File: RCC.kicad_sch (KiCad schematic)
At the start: 42 parts, among them J1 Battery, J2 USB_C_Receptacle_USB2.0_16P, J3 Conn_01x07, J4 Conn_01x04_Pin, SW2 SW_Push, U1 BQ24040DGQR, U2 ESD7104MUTAG, U3 TLV75801PDRV, U5 STM32L412KBTx

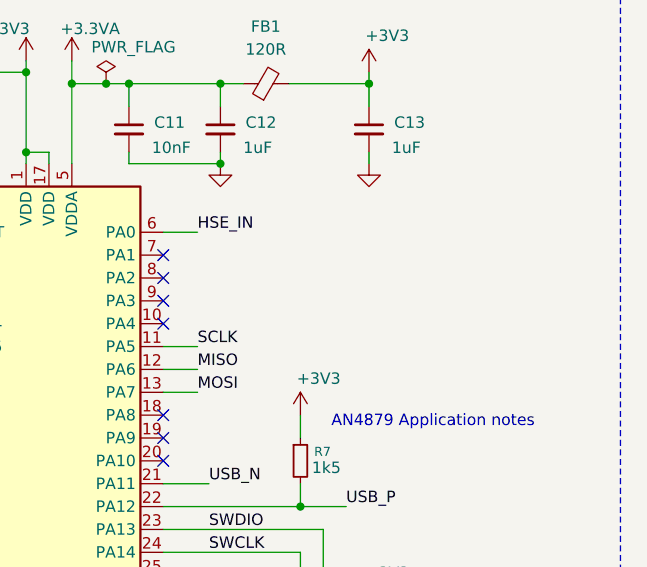
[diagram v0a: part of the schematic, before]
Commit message: Add crystal in schematic and pcb
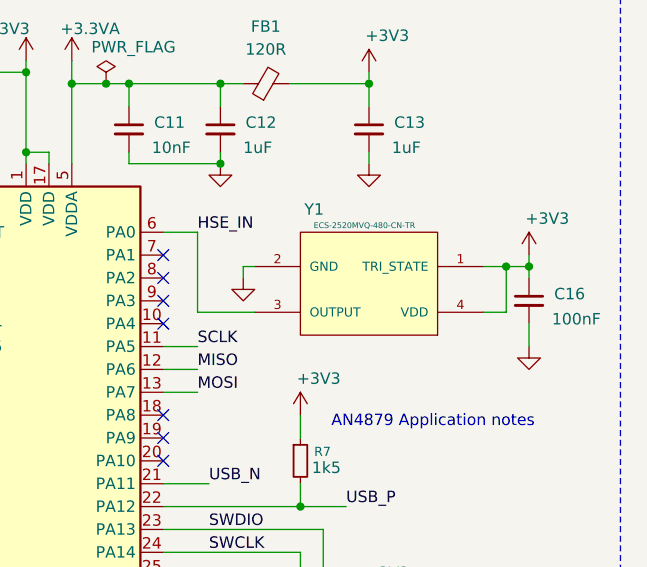
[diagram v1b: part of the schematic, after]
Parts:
- added C16: 100nF, Capacitor_SMD:C_0603_1608Metric, symbol Device:C_Small
- added Y1: ECS-2520MVQ-480-CN-TR, ECS_2520MVQ_480_CN_TR:OSC_ECS-2520S25-250-FN-TR, symbol ECS-2520MVQ-480-CN-TR:ECS-2520MVQ-480-CN-TR
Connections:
- net +3V3: now also C16.1, Y1.1 (TRI_STATE), Y1.4 (VDD)
- net GND: now also C16.2, Y1.2 (GND)
- net HSE_IN: now also Y1.3 (OUTPUT)

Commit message: Finalise PCB and add 3d models
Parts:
- added D4: LED_Small, LED_SMD:LED_0603_1608Metric, symbol Device:LED_Small
- J4: footprint Connector_JST:JST_EH_B4B-EH-A_1x04_P2.50mm_Vertical -> Connector_JST:JST_EH_S4B-EH_1x04_P2.50mm_Horizontal
- R11: value 0 -> 1k
- R7: now not fitted
- U2: footprint ESD7104:UDFN10_ONS -> UDFN10_ONS
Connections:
- net CHG_STATUS: now also U5.27 (PB4)
- net DIS_CS: now also U5.30 (PB7)
- net DIS_DC: now also U5.29 (PB6)
- net DIS_RST: now also U5.28 (PB5)
- net GND: now also D4.1 (K); no longer R11.2
- net GYRO_CS: now also U5.14 (PB0)
- net GY_INT1: now also U5.10 (PA4)
- net GY_INT2: now also U5.15 (PB1)
- net SWCLK: now also J4.2 (Pin_2); no longer J4.3 (Pin_3)
- net SWDIO: now also J4.3 (Pin_3); no longer J4.2 (Pin_2)
- net VBUS: now also U2.5 (I/O), U2.6 (NC); no longer U2.4 (I/O), U2.7 (NC)
- net at J2.S1 (SHIELD): no longer R11.1
- net TEST_LED: now reaches U5.18 (PA8)
- net TEST_LED: now also R11.2
- new net: D4.2 (A), R11.1
- no-connect marks 25 -> 19
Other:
- note removed: "Connect CC line? 5k11"
- note removed: "TODO: - SPI CSs - GPIOs (display and inter - HSE clock (0-48MHz) - Status LEDs"
- note removed: "TODO: Calculate resistance and cutoff load when charging"
- moved on the sheet: C1, C10, C11, C12, C13, C14, C15, C16, C2, C8, C9, D2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

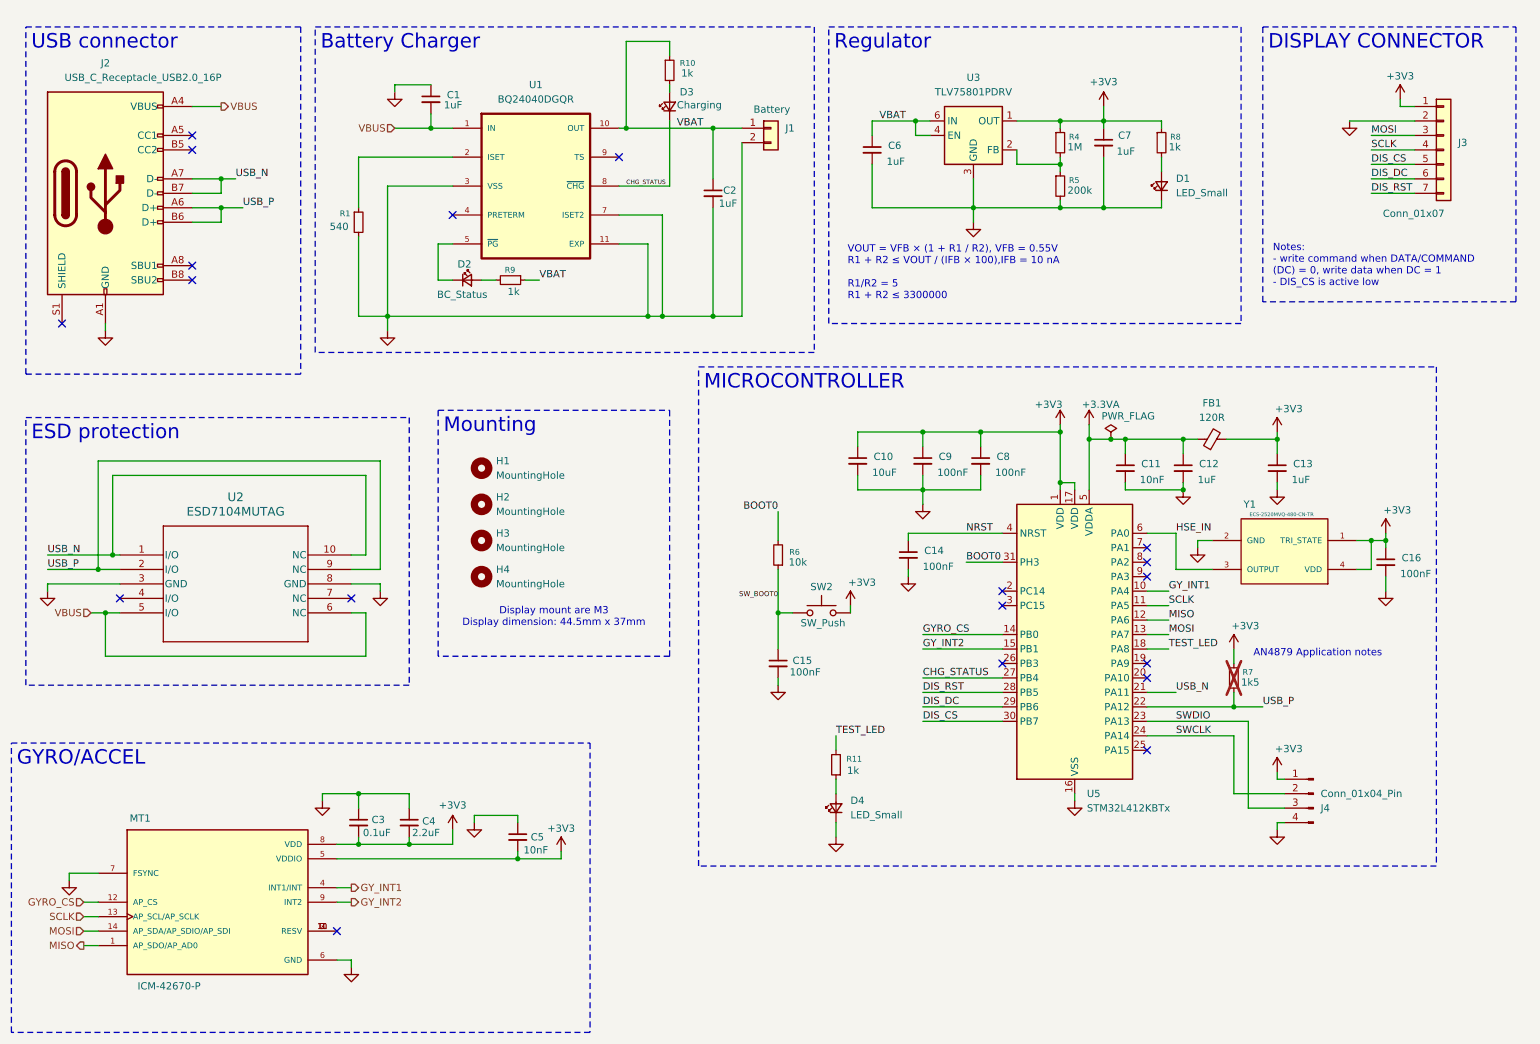
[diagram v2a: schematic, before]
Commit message: Change connectors to jst-ph
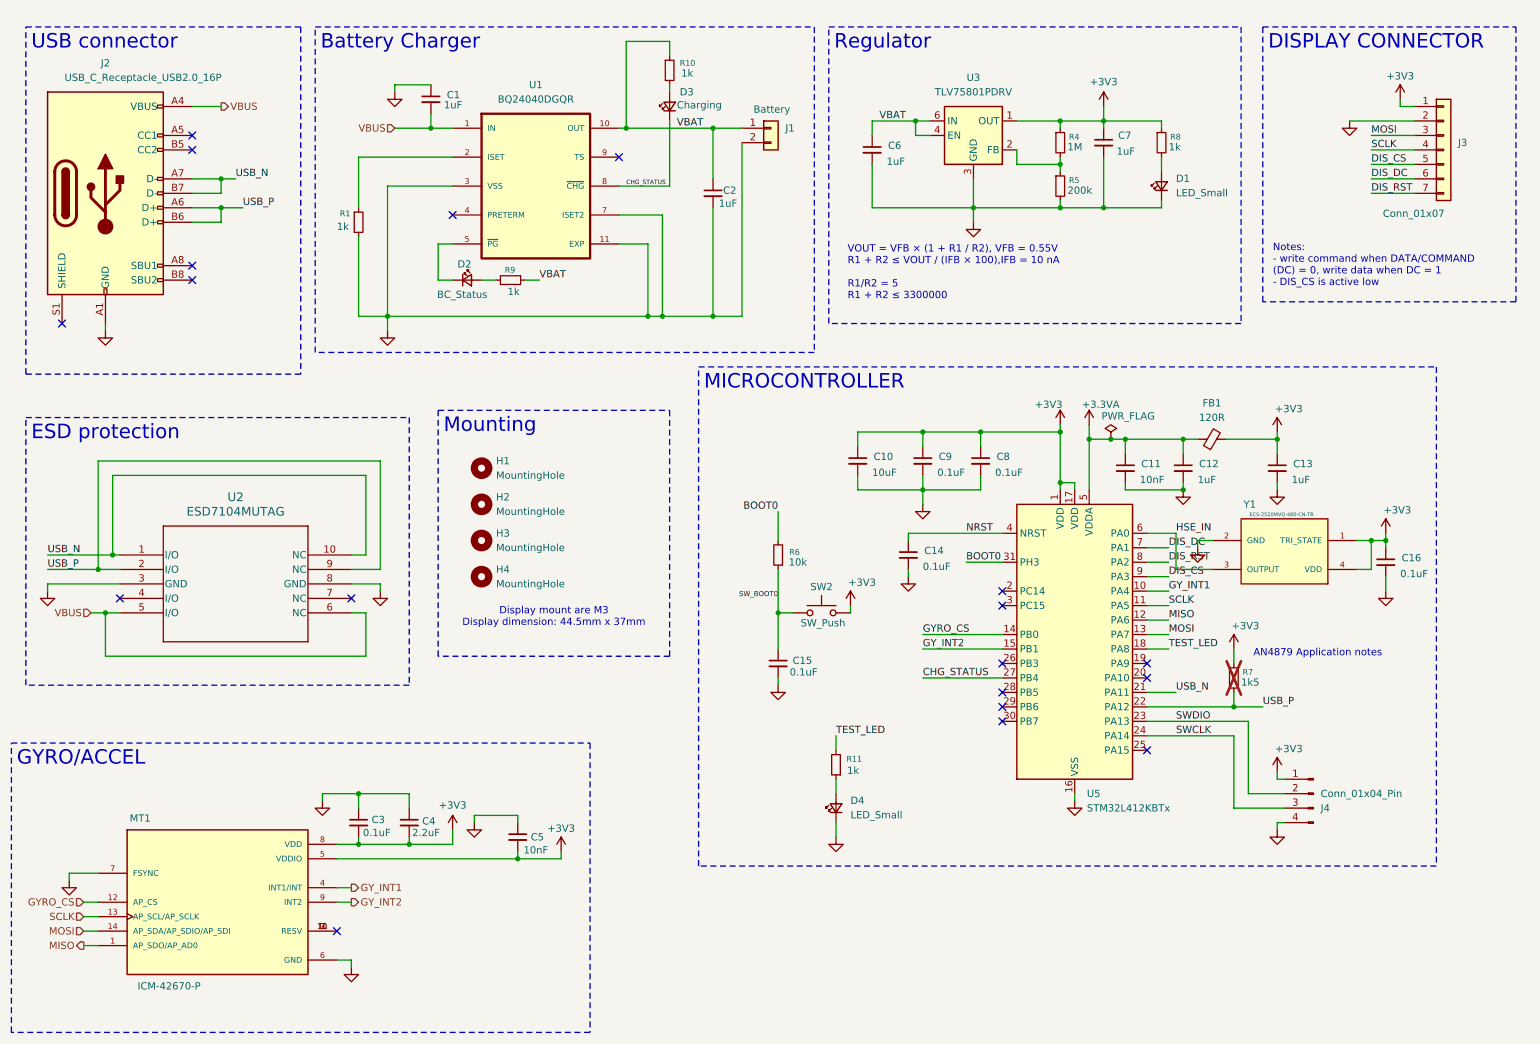
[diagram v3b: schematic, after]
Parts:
- C14, C15, C16, C8, C9: value 100nF -> 0.1uF
- J1: footprint Connector_JST:JST_EH_S2B-EH_1x02_P2.50mm_Horizontal -> Connector_JST:JST_PH_S2B-PH-K_1x02_P2.00mm_Horizontal
- J3: footprint Connector_JST:JST_EH_S7B-EH_1x07_P2.50mm_Horizontal -> Connector_JST:JST_PH_S7B-PH-K_1x07_P2.00mm_Horizontal
- J4: footprint Connector_JST:JST_EH_S4B-EH_1x04_P2.50mm_Horizontal -> Connector_JST:JST_PH_S4B-PH-K_1x04_P2.00mm_Horizontal
- R1: value 540 -> 1k
- U2: footprint UDFN10_ONS -> ESD7104:UDFN10_ONS
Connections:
- net DIS_CS: now also U5.9 (PA3); no longer U5.30 (PB7)
- net DIS_DC: now also U5.7 (PA1); no longer U5.29 (PB6)
- net DIS_RST: now also U5.8 (PA2); no longer U5.28 (PB5)
- net SWCLK: now also J4.3 (Pin_3); no longer J4.2 (Pin_2)
- net SWDIO: now also J4.2 (Pin_2); no longer J4.3 (Pin_3)
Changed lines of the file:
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@@
 	)
 	(no_connect
+		(at 189.23 135.89)
+	)
+	(no_connect
 		(at 214.63 143.51)
 	)
 	(no_connect
+		(at 189.23 133.35)
+	)
+	(no_connect
 		(at 46.99 60.96)
 	)
@@
 	)
 	(no_connect
-		(at 214.63 107.95)
-	)
-	(no_connect
 		(at 92.71 49.53)
 	)
@@
 	)
 	(no_connect
-		(at 214.63 113.03)
-	)
-	(no_connect
 		(at 46.99 38.1)
 	)
@@
 	)
 	(no_connect
-		(at 214.63 110.49)
+		(at 189.23 128.27)
 	)
 	(no_connect
-		(at 189.23 128.27)
+		(at 189.23 138.43)
 	)
 	(no_connect
@@
 	(wire
 		(pts
+			(xy 229.87 153.67) (xy 238.76 153.67)
+		)
+		(stroke
+			(width 0)
+			(type default)
+		)
+	)
+	(wire
+		(pts
 			(xy 185.42 87.63) (xy 185.42 90.17)
 		)
@@
 	(wire
 		(pts
-			(xy 175.26 135.89) (xy 189.23 135.89)
-		)
-		(stroke
-			(width 0)
-			(type default)
-		)
-	)
-	(wire
-		(pts
 			(xy 175.26 123.19) (xy 189.23 123.19)
 		)
@@
 	(wire
 		(pts
+			(xy 214.63 113.03) (xy 218.44 113.03)
+		)
+		(stroke
+			(width 0)
+			(type default)
+		)
+	)
+	(wire
+		(pts
 			(xy 163.83 97.79) (xy 175.26 97.79)
 		)
@@
 	(wire
 		(pts
+			(xy 232.41 138.43) (xy 232.41 151.13)
+		)
+		(stroke
+			(width 0)
+			(type default)
+		)
+	)
+	(wire
+		(pts
 			(xy 149.86 101.6) (xy 149.86 106.68)
 		)
@@
 	(wire
 		(pts
+			(xy 214.63 110.49) (xy 218.44 110.49)
+		)
+		(stroke
+			(width 0)
+			(type default)
+		)
+	)
+	(wire
+		(pts
 			(xy 172.72 111.76) (xy 172.72 113.03)
 		)
@@
 	(wire
 		(pts
-			(xy 90.17 54.61) (xy 90.17 60.96)
+			(xy 232.41 151.13) (xy 238.76 151.13)
 		)
 		(stroke
@@
 	(wire
 		(pts
-			(xy 214.63 120.65) (xy 218.44 120.65)
+			(xy 90.17 54.61) (xy 90.17 60.96)
 		)
 		(stroke
@@
 	(wire
 		(pts
-			(xy 21.59 111.76) (xy 30.48 111.76)
+			(xy 214.63 120.65) (xy 218.44 120.65)
 		)
 		(stroke
@@
 	(wire
 		(pts
-			(xy 92.71 39.37) (xy 76.2 39.37)
+			(xy 21.59 111.76) (xy 30.48 111.76)
 		)
 		(stroke
@@
 	(wire
 		(pts
-			(xy 127 54.61) (xy 121.92 54.61)
+			(xy 92.71 39.37) (xy 76.2 39.37)
 		)
 		(stroke
@@
 	(wire
 		(pts
-			(xy 104.14 161.29) (xy 104.14 162.56)
+			(xy 127 54.61) (xy 121.92 54.61)
 		)
 		(stroke
@@
 	(wire
 		(pts
-			(xy 232.41 153.67) (xy 238.76 153.67)
+			(xy 104.14 161.29) (xy 104.14 162.56)
 		)
 		(stroke
@@
 	(wire
 		(pts
-			(xy 123.19 34.29) (xy 138.43 34.29)
+			(xy 214.63 107.95) (xy 218.44 107.95)
 		)
 		(stroke
@@
 	(wire
 		(pts
-			(xy 229.87 140.97) (xy 229.87 151.13)
+			(xy 123.19 34.29) (xy 138.43 34.29)
 		)
 		(stroke
@@
 	(wire
 		(pts
-			(xy 214.63 123.19) (xy 218.44 123.19)
+			(xy 229.87 140.97) (xy 229.87 153.67)
 		)
 		(stroke
@@
 	(wire
 		(pts
-			(xy 34.29 114.3) (xy 21.59 114.3)
+			(xy 214.63 123.19) (xy 218.44 123.19)
 		)
 		(stroke
@@
 	(wire
 		(pts
-			(xy 175.26 133.35) (xy 189.23 133.35)
+			(xy 34.29 114.3) (xy 21.59 114.3)
 		)
 		(stroke
@@
 	(wire
 		(pts
-			(xy 175.26 138.43) (xy 189.23 138.43)
-		)
-		(stroke
-			(width 0)
-			(type default)
-		)
-	)
-	(wire
-		(pts
-			(xy 229.87 151.13) (xy 238.76 151.13)
-		)
-		(stroke
-			(width 0)
-			(type default)
-		)
-	)
-	(wire
-		(pts
 			(xy 237.49 147.32) (xy 237.49 148.59)
 		)
@@
 	(wire
 		(pts
-			(xy 229.87 135.89) (xy 234.95 135.89)
-		)
-		(stroke
-			(width 0)
-			(type default)
-		)
-	)
-	(wire
-		(pts
 			(xy 207.01 33.02) (xy 217.17 33.02)
 		)
@@
 	(wire
 		(pts
-			(xy 232.41 138.43) (xy 232.41 153.67)
-		)
-		(stroke
-			(width 0)
-			(type default)
-		)
-	)
-	(wire
-		(pts
 			(xy 229.87 133.35) (xy 229.87 135.89)
 		)
@@
 	(wire
 		(pts
-			(xy 214.63 138.43) (xy 232.41 138.43)
+			(xy 229.87 135.89) (xy 234.95 135.89)
 		)
 		(stroke
@@
 	(wire
 		(pts
+			(xy 214.63 138.43) (xy 232.41 138.43)
+		)
+		(stroke
+			(width 0)
+			(type default)
+		)
+	)
+	(wire
+		(pts
 			(xy 226.06 106.68) (xy 223.52 106.68)
 		)
@@
 		)
 	)
-	(label "DIS_DC"
-		(at 175.26 135.89 0)
+	(label "DIS_RST"
+		(at 218.44 110.49 0)
 		(effects
 			(font
@@
 		)
 	)
-	(label "DIS_RST"
-		(at 175.26 133.35 0)
+	(label "DIS_CS"
+		(at 218.44 113.03 0)
 		(effects
 			(font
@@
 		)
 	)
-	(label "DIS_CS"
-		(at 175.26 138.43 0)
+	(label "DIS_DC"
+		(at 218.44 107.95 0)
 		(effects
 			(font
@@
 			)
 		)
-		(property "Footprint" "Connector_JST:JST_EH_S2B-EH_1x02_P2.50mm_Horizontal"
+		(property "Footprint" "Connector_JST:JST_PH_S2B-PH-K_1x02_P2.00mm_Horizontal"
 			(at 148.59 34.29 0)
 			(effects
@@
 			)
 		)
-		(property "Value" "100nF"
+		(property "Value" "0.1uF"
 			(at 259.08 112.522 0)
 			(effects
@@
 			)
 		)
-		(property "Value" "100nF"
+		(property "Value" "0.1uF"
 			(at 151.892 129.794 0)
 			(effects
@@
 			)
 		)
-		(property "Value" "100nF"
+		(property "Value" "0.1uF"
 			(at 187.96 94.742 0)
 			(effects
@@
 			)
 		)
-		(property "Footprint" "Connector_JST:JST_EH_S4B-EH_1x04_P2.50mm_Horizontal"
+		(property "Footprint" "Connector_JST:JST_PH_S4B-PH-K_1x04_P2.00mm_Horizontal"
 			(at 243.84 151.13 0)
 			(effects
@@
 			)
 		)
-		(property "Value" "540"
-			(at 71.12 51.562 0)
+		(property "Value" "1k"
+			(at 72.39 51.562 0)
 			(effects
 				(font
@@
 			)
 		)
-		(property "Value" "100nF"
+		(property "Value" "0.1uF"
 			(at 177.8 94.742 0)
 			(effects
@@
 			)
 		)
-		(property "Footprint" "Connector_JST:JST_EH_S7B-EH_1x07_P2.50mm_Horizontal"
+		(property "Footprint" "Connector_JST:JST_PH_S7B-PH-K_1x07_P2.00mm_Horizontal"
 			(at 266.7 38.1 0)
 			(effects
@@
 			)
 		)
-		(property "Value" "100nF"
+		(property "Value" "0.1uF"
 			(at 175.26 111.252 0)
 			(effects
@@
 			)
 		)
-		(property "Footprint" "UDFN10_ONS"
+		(property "Footprint" "ESD7104:UDFN10_ONS"
 			(at 34.29 109.22 0)
 			(effects

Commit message: Add termination resistor to spi and change esd protection
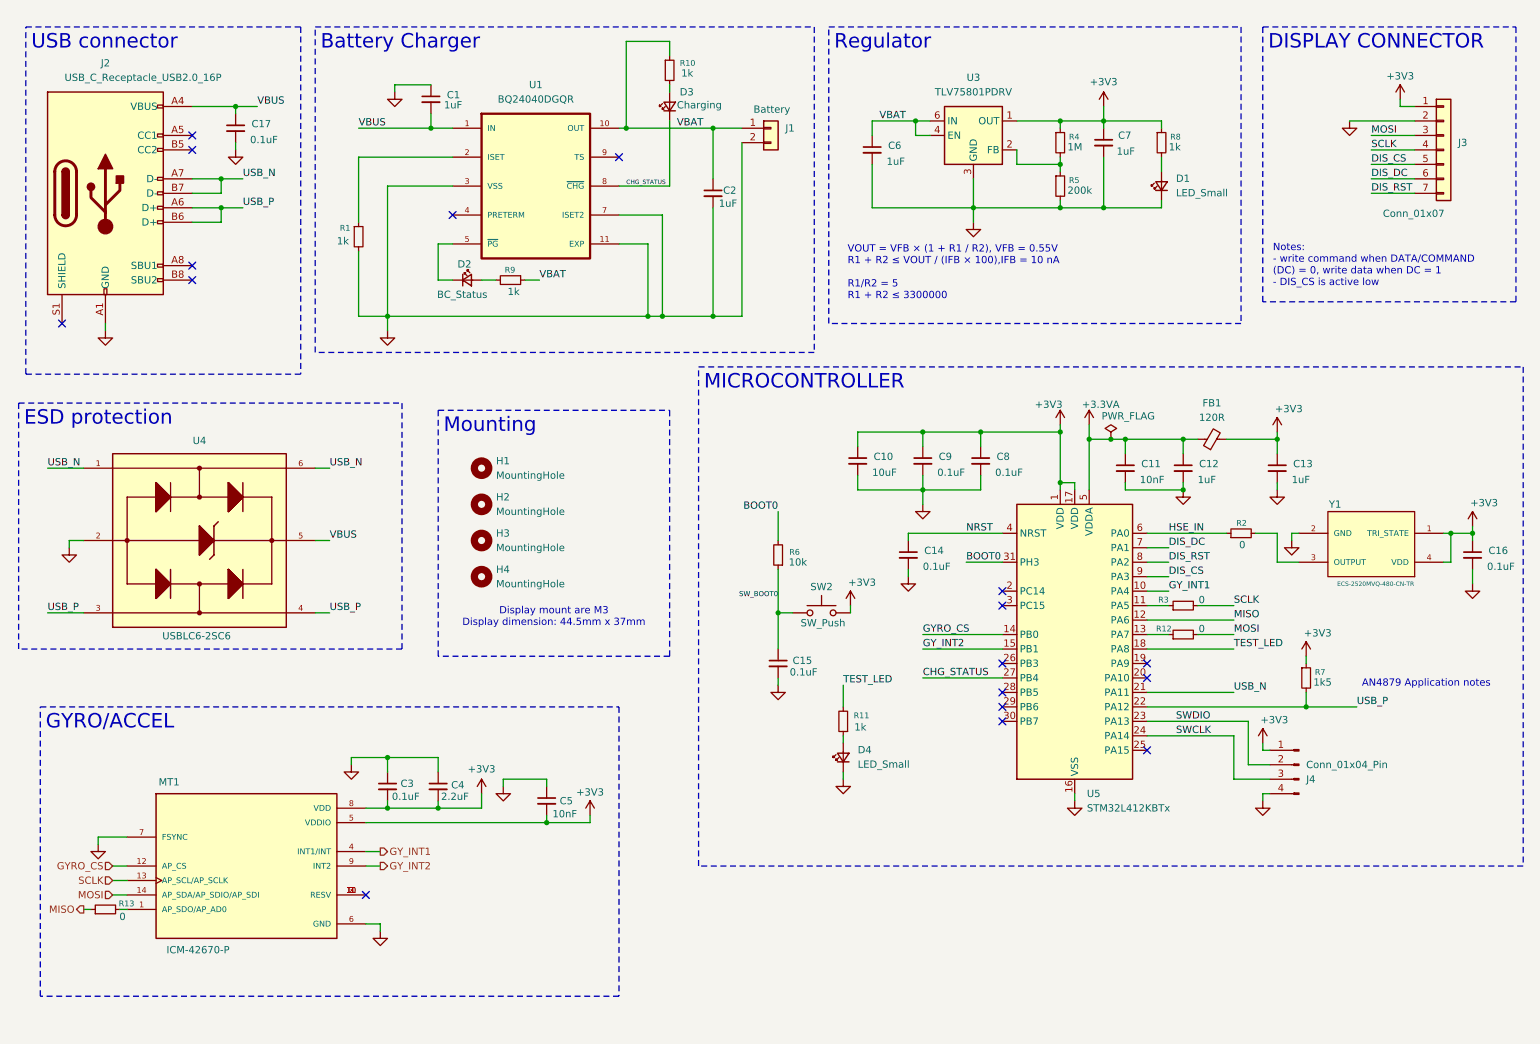
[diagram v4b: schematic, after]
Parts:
- removed U2: ESD7104MUTAG, ESD7104:UDFN10_ONS, symbol ESD7104:ESD7104MUTAG
- added C17: 0.1uF, Capacitor_SMD:C_0603_1608Metric, symbol Device:C_Small
- added R12, R13, R2, R3: 0, Resistor_SMD:R_0603_1608Metric, symbol Device:R_Small
- added U4: USBLC6-2SC6, USBLC6-2SC6:SOT95P280X145-6N, symbol USBLC6-2SC6:USBLC6-2SC6
- R7: now fitted
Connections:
- net GND: now also C17.2, U4.2
- net HSE_IN: now also R2.1; no longer Y1.3 (OUTPUT)
- net MISO: now also R13.1; no longer MT1.1 (AP_SDO/AP_AD0)
- net MOSI: now also R12.2; no longer U5.13 (PA7)
- net SCLK: now also R3.2; no longer U5.11 (PA5)
- net USB_N: now also U4.1, U4.6
- net USB_P: now also U4.3, U4.4
- net VBUS: now also C17.1, U4.5
- new net: MT1.1 (AP_SDO/AP_AD0), R13.2
- new net: R12.1, U5.13 (PA7)
- new net: R2.2, Y1.3 (OUTPUT)
- new net: R3.1, U5.11 (PA5)
- no-connect marks 19 -> 17
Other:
- moved on the sheet: C16, C3, C4, C5, D4, J4, MT1, R1, R11, Y1
